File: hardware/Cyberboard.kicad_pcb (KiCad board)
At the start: 2 copper layers, 21 x 51 mm, 60 parts, among them CN1 B2B-XH-A (LF)(SN), J1 Conn_01x20, J2 Conn_01x20, SW1 SW_Push, SW2 SW_Push, U1 TPS630701RNMR, U2 NX2012SA-32.768KHZ-STD-MUB-2, U3 XL-1005UBC_C22355736, U5 BQ24074RGT, U6 STM32WB55CGUx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

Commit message: finished layout
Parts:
- removed U6: STM32WB55CGUx, Package_DFN_QFN:QFN-48-1EP_7x7mm_P0.5mm_EP5.6x5.6mm
- added U4: STM32WB55RGVx, Package_DFN_QFN:QFN-68-1EP_8x8mm_P0.4mm_EP6.4x6.4mm, F.Cu at (146.0, 90.9)
- C1, C10, C11, C12, C18, C19, C2, C20, C3, C4, C8, C9, LED1, R10, R3, R4, R5, R6, R7, R8, R9, U3, U5: moved to B.Cu
- C13, C5, C7: footprint Capacitor_SMD:C_0402_1005Metric -> Capacitor_SMD:C_0603_1608Metric; moved to B.Cu
- C21, C22, C25, C26, C27, C28: footprint Capacitor_SMD:C_0805_2012Metric -> Capacitor_SMD:C_0603_1608Metric
- C6: value 10nF -> 100nF; moved to B.Cu
- L1, L2: footprint Inductor_SMD:L_0603_1608Metric -> Inductor_SMD:L_0805_2012Metric; moved to B.Cu
- moved C20 114.5 mm to (145.5, 65.7), turned to 180 degrees
- moved R8 113.1 mm to (143.0, 66.6)
- moved R5 111.0 mm to (143.0, 67.6)
- moved R3 109.6 mm to (143.0, 68.7)
- moved U5 109.5 mm to (146.2, 68.8), turned to -90 degrees
- moved LED1 109.2 mm to (149.8, 69.0)
- moved R6 109.2 mm to (152.0, 69.0)
- moved C18 107.1 mm to (143.2, 70.8), turned to -90 degrees
- moved U3 105.7 mm to (149.8, 70.5), turned to 0 degrees
- moved R4 105.5 mm to (144.9, 72.1), turned to 90 degrees
- moved C19 104.7 mm to (147.0, 71.9), turned to 0 degrees
- moved R7 102.9 mm to (152.0, 70.5), turned to 0 degrees
- moved C16 100.1 mm to (141.9, 81.9)
- moved CN1 98.6 mm to (146.2, 64.0), turned to 180 degrees
- moved U2 98.6 mm to (142.7, 83.9), turned to 180 degrees
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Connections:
- J1 pad 1: unconnected-(J1-Pin_1-Pad1) -> /GPIO16
- J1 pad 10: unconnected-(J1-Pin_10-Pad10) -> /GPIO23
- J1 pad 11: unconnected-(J1-Pin_11-Pad11) -> /GPIO24
- J1 pad 12: unconnected-(J1-Pin_12-Pad12) -> /GPIO25
- J1 pad 13: unconnected-(J1-Pin_13-Pad13) -> GND
- J1 pad 14: unconnected-(J1-Pin_14-Pad14) -> /GPIO26
- J1 pad 15: unconnected-(J1-Pin_15-Pad15) -> /GPIO27
- J1 pad 16: unconnected-(J1-Pin_16-Pad16) -> +3.3V
- J1 pad 17: unconnected-(J1-Pin_17-Pad17) -> /GPIO28
- J1 pad 18: unconnected-(J1-Pin_18-Pad18) -> GND
- J1 pad 19: unconnected-(J1-Pin_19-Pad19) -> /GPIO29
- J1 pad 2: unconnected-(J1-Pin_2-Pad2) -> /GPIO17
- J1 pad 20: unconnected-(J1-Pin_20-Pad20) -> VBUS
- J1 pad 3: unconnected-(J1-Pin_3-Pad3) -> GND
- J1 pad 4: unconnected-(J1-Pin_4-Pad4) -> /GPIO18
- J1 pad 5: unconnected-(J1-Pin_5-Pad5) -> /GPIO19
- J1 pad 6: unconnected-(J1-Pin_6-Pad6) -> /GPIO20
- J1 pad 7: unconnected-(J1-Pin_7-Pad7) -> /GPIO21
- J1 pad 8: unconnected-(J1-Pin_8-Pad8) -> GND
- J1 pad 9: unconnected-(J1-Pin_9-Pad9) -> /GPIO22
- J2 pad 1: unconnected-(J2-Pin_1-Pad1) -> /GPIO15
- J2 pad 10: unconnected-(J2-Pin_10-Pad10) -> /GPIO8
- J2 pad 11: unconnected-(J2-Pin_11-Pad11) -> /GPIO7
- J2 pad 12: unconnected-(J2-Pin_12-Pad12) -> /GPIO6
- J2 pad 13: unconnected-(J2-Pin_13-Pad13) -> GND
- J2 pad 14: unconnected-(J2-Pin_14-Pad14) -> /GPIO5
- J2 pad 15: unconnected-(J2-Pin_15-Pad15) -> /GPIO4
- J2 pad 16: unconnected-(J2-Pin_16-Pad16) -> /GPIO3
- J2 pad 17: unconnected-(J2-Pin_17-Pad17) -> /GPIO2
- J2 pad 18: unconnected-(J2-Pin_18-Pad18) -> GND
- J2 pad 19: unconnected-(J2-Pin_19-Pad19) -> /GPIO1
- J2 pad 2: unconnected-(J2-Pin_2-Pad2) -> /GPIO14
- J2 pad 20: unconnected-(J2-Pin_20-Pad20) -> /GPIO0
- J2 pad 3: unconnected-(J2-Pin_3-Pad3) -> GND
- J2 pad 4: unconnected-(J2-Pin_4-Pad4) -> /GPIO13
- J2 pad 5: unconnected-(J2-Pin_5-Pad5) -> /GPIO12
- J2 pad 6: unconnected-(J2-Pin_6-Pad6) -> /GPIO11
- J2 pad 7: unconnected-(J2-Pin_7-Pad7) -> /GPIO10
- J2 pad 8: unconnected-(J2-Pin_8-Pad8) -> GND
- J2 pad 9: unconnected-(J2-Pin_9-Pad9) -> /GPIO9
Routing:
- net GND: vias 0 -> 4

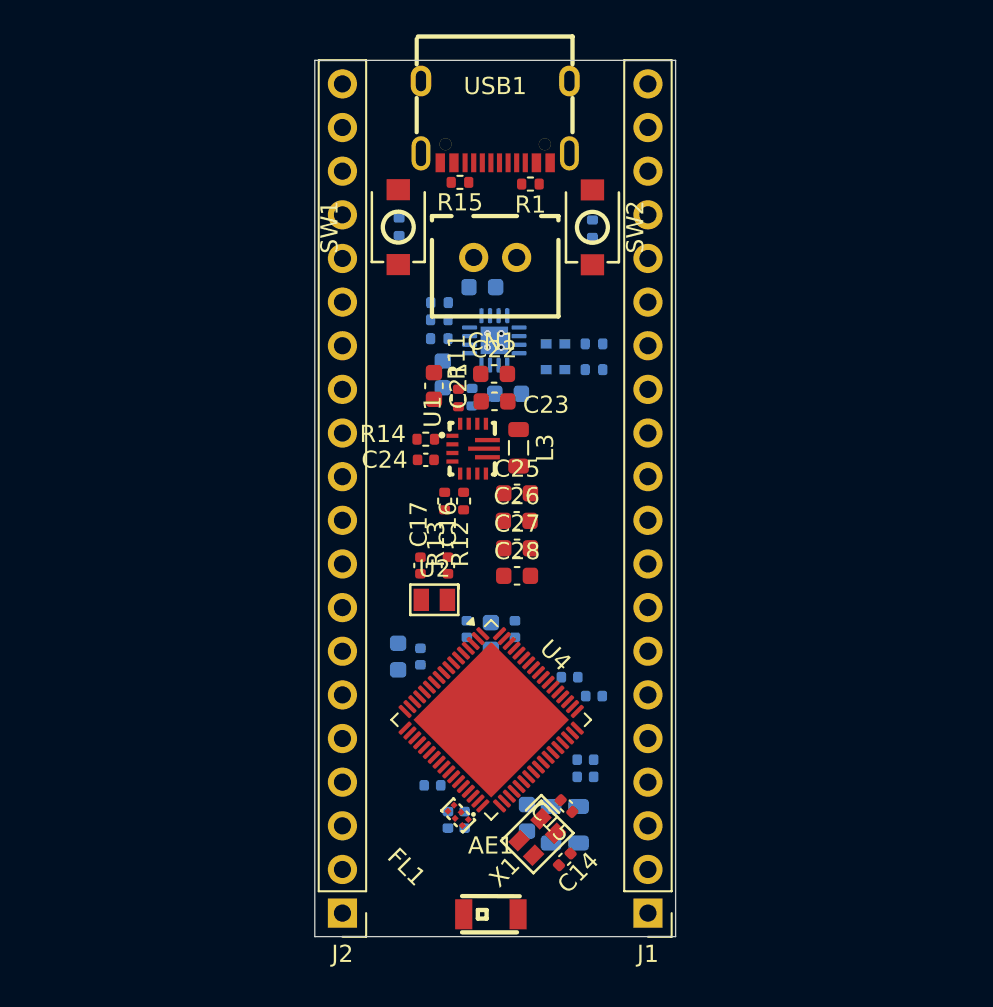
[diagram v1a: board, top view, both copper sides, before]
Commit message: add readme and also blender files
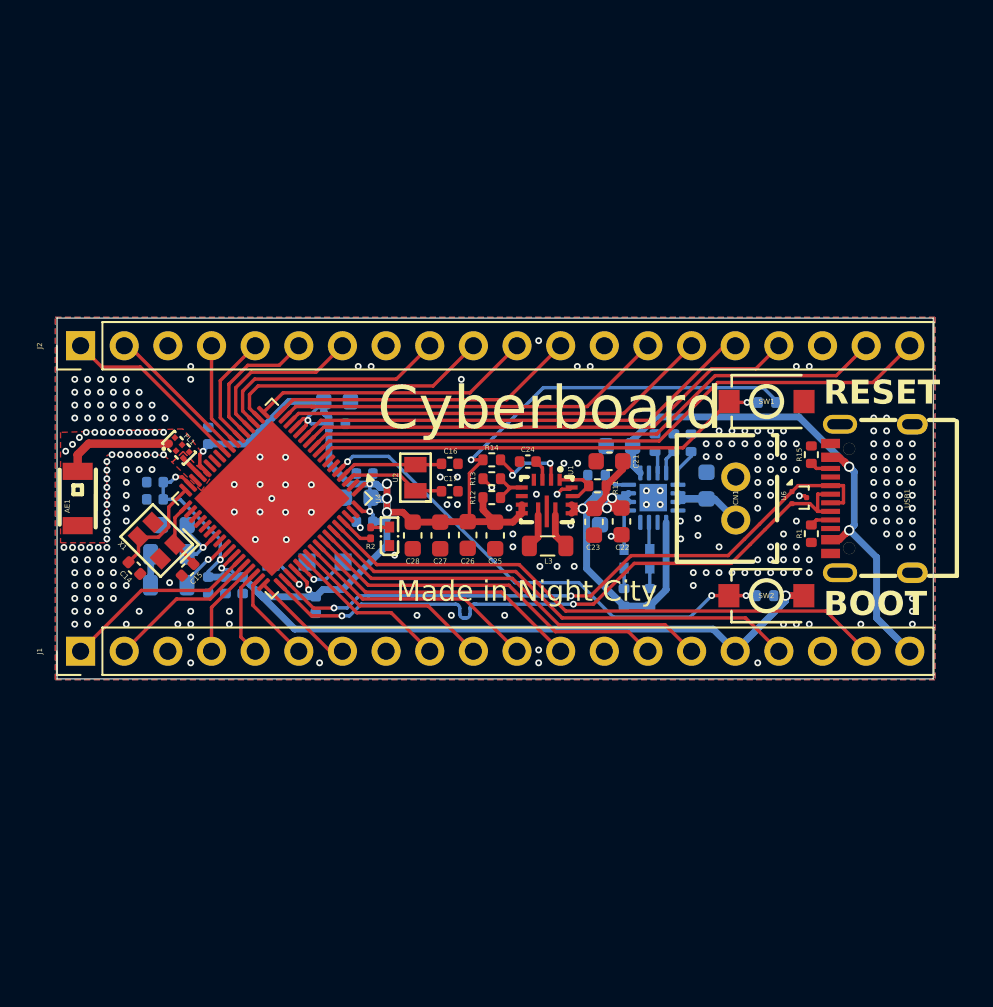
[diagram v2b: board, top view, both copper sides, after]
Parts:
- added R2: 47, Resistor_SMD:R_0201_0603Metric, F.Cu at (139.0, 80.0)
- added TP1: TestPoint, TestPoint:TestPoint_Pad_1.0x1.0mm, B.Cu at (133.2, 81.7)
- added TP2: TestPoint, TestPoint:TestPoint_Pad_1.0x1.0mm, B.Cu at (137.4, 81.7)
- added TP3: TestPoint, TestPoint:TestPoint_Pad_1.0x1.0mm, B.Cu at (135.3, 81.7)
- added U6: TPD2EUSB30, Package_TO_SOT_SMD:Texas_DRT-3, F.Cu at (163.9, 78.0)
- added U7: SZYY0402Y_C434450, lcsc:LED0402-FD_YELLOW, F.Cu at (140.1, 80.2)
- moved J2 36.4 mm to (122.1, 69.1), turned to 90 degrees
- moved J1 36.4 mm to (122.1, 86.9), turned to 90 degrees
- moved AE1 34.1 mm to (122.0, 78.0), turned to -90 degrees
- moved USB1 31.0 mm to (168.2, 78.0), turned to 90 degrees
- moved C14 30.2 mm to (125.2, 82.0), turned to -45 degrees
- moved X1 28.1 mm to (126.5, 80.5), turned to 135 degrees
- moved L1 27.6 mm to (127.2, 83.0), turned to 0 degrees
- moved L2 27.2 mm to (127.3, 81.2), turned to 180 degrees
- moved FL1 26.9 mm to (127.8, 75.0), turned to -45 degrees
- moved C13 26.7 mm to (127.5, 79.5), turned to 180 degrees
- moved R1 26.1 mm to (164.7, 80.0), turned to -90 degrees
- moved C11 26.0 mm to (126.5, 77.0), turned to 180 degrees
- moved C15 26.0 mm to (128.3, 82.2), turned to -135 degrees
- moved C10 25.9 mm to (126.5, 78.0), turned to 180 degrees
- moved R15 25.9 mm to (164.7, 75.5), turned to 90 degrees
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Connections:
- U4 pad 65: unconnected-(U4-PB5-Pad65) -> /LED
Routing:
- net +3.3V: track 0.00 -> 133.0 mm, vias 0 -> 13
- net /DN: track 0.00 -> 38.6 mm, vias 0 -> 2
- net /DP: track 0.00 -> 37.9 mm, vias 0 -> 2
- net /GPIO0: track 0.00 -> 36.9 mm
- net /GPIO1: track 0.00 -> 34.6 mm
- net /GPIO29: track 0.00 -> 33.7 mm
- net VBUS: track 0.00 -> 31.7 mm, vias 0 -> 2
- net /GPIO2: track 0.00 -> 29.6 mm
- net VCC: track 0.00 -> 29.2 mm, vias 0 -> 3
- net /BOOT: track 0.00 -> 29.1 mm, vias 0 -> 3
- net /GPIO28: track 0.00 -> 28.8 mm
- net /GPIO3: track 0.00 -> 27.3 mm
- net /RESET: track 0.00 -> 26.7 mm, vias 0 -> 1
- net /GPIO4: track 0.00 -> 25.2 mm
- net /GPIO27: track 0.00 -> 23.9 mm
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- added copper zone on B.Cu, net GND
- added copper zone on F.Cu, net GND
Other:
- board size 21 x 51 mm -> 51 x 21 mm
- board text added: "@NotARoomba"
- board text added: "BOOT"
- board text added: "CHGING"
- board text added: "Cyberboard"
- board text added: "Made in Night City"
- board text added: "READY"
- board text added: "RESET"
- board text added: "SWCLK"
- board text added: "SWD"

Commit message: add order and prod files
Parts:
- R2: value 47 -> 150
- R5: value 1.13 -> 1.13K
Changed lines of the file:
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@@
 			)
 		)
-		(property "Value" "47"
+		(property "Value" "150"
 			(at 3 0.9 90)
 			(layer "F.Fab")
@@
 			)
 		)
-		(property "Value" "1.13"
+		(property "Value" "1.13K"
 			(at 0 -1.17 90)
 			(layer "B.Fab")
@@
 				(justify mirror)
 			)
-			(render_cache "1.13" 90
+			(render_cache "1.13K" 90
 				(polygon
 					(pts
-						(xy 157.9445 74.503364) (xy 157.9445 74.458814) (xy 157.734646 74.458814) (xy 157.734646 74.408988)
-						(xy 157.692441 74.408988) (xy 157.692441 74.503364)
+						(xy 157.9445 74.39023) (xy 157.9445 74.34568) (xy 157.734646 74.34568) (xy 157.734646 74.295854)
+						(xy 157.692441 74.295854) (xy 157.692441 74.39023)
 					)
 				)
 				(polygon
 					(pts
-						(xy 157.9445 74.655478) (xy 157.9445 74.603894) (xy 157.891743 74.603894) (xy 157.891743 74.655478)
+						(xy 157.9445 74.542344) (xy 157.9445 74.49076) (xy 157.891743 74.49076) (xy 157.891743 74.542344)
 					)
 				)
 				(polygon
 					(pts
-						(xy 157.9445 74.833092) (xy 157.9445 74.788542) (xy 157.734646 74.788542) (xy 157.734646 74.738716)
-						(xy 157.692441 74.738716) (xy 157.692441 74.833092)
+						(xy 157.9445 74.719958) (xy 157.9445 74.675408) (xy 157.734646 74.675408) (xy 157.734646 74.625582)
+						(xy 157.692441 74.625582) (xy 157.692441 74.719958)
 					)
 				)
 				(polygon
 					(pts
-						(xy 157.887273 75.053203) (xy 157.853605 75.053203) (xy 157.851535 75.052782) (xy 157.842394 75.04551)
-						(xy 157.838717 75.040776) (xy 157.837814 75.037834) (xy 157.837814 75.037413) (xy 157.837814 74.98462)
-						(xy 157.795609 74.98462) (xy 157.795609 75.037725) (xy 157.795609 75.038146) (xy 157.7947 75.041106)
-						(xy 157.790993 75.045876) (xy 157.78176 75.053203) (xy 157.779654 75.053203) (xy 157.749429 75.053203)
-						(xy 157.747322 75.052782) (xy 157.737888 75.045107) (xy 157.73435 75.040379) (xy 157.733474 75.037413)
-						(xy 157.733474 74.990061) (xy 157.733895 74.988375) (xy 157.737079 74.982968) (xy 157.742505 74.976413)
-						(xy 157.748936 74.970897) (xy 157.755309 74.967822) (xy 157.743549 74.924976) (xy 157.72556 74.935051)
-						(xy 157.709092 74.950196) (xy 157.698696 74.963948) (xy 157.693046 74.976641) (xy 157.691269 74.988705)
-						(xy 157.691269 75.038201) (xy 157.692312 75.048811) (xy 157.695382 75.058528) (xy 157.700519 75.067565)
-						(xy 157.711092 75.0797) (xy 157.723618 75.090206) (xy 157.735634 75.095845) (xy 157.749264 75.097753)
-						(xy 157.780771 75.097753) (xy 157.79274 75.096009) (xy 157.804526 75.090616) (xy 157.816492 75.080937)
-						(xy 157.828451 75.090589) (xy 157.840359 75.095996) (xy 157.852579 75.097753) (xy 157.887786 75.097753)
-						(xy 157.901398 75.095845) (xy 157.913395 75.090206) (xy 157.92554 75.07949) (xy 157.936439 75.067565)
-						(xy 157.941566 75.058529) (xy 157.94463 75.048812) (xy 157.945672 75.038201) (xy 157.945672 74.988705)
-						(xy 157.94385 74.976228) (xy 157.938113 74.963384) (xy 157.927649 74.949757) (xy 157.911179 74.935051)
-						(xy 157.900508 74.928054) (xy 157.89308 74.924555) (xy 157.881851 74.967401) (xy 157.896679 74.979139)
-						(xy 157.903467 74.987972) (xy 157.903467 74.990061) (xy 157.903467 75.037725) (xy 157.90261 75.04037)
-						(xy 157.898905 75.045253) (xy 157.889343 75.053203)
+						(xy 157.887273 74.940069) (xy 157.853605 74.940069) (xy 157.851535 74.939648) (xy 157.842394 74.932376)
+						(xy 157.838717 74.927642) (xy 157.837814 74.9247) (xy 157.837814 74.924279) (xy 157.837814 74.871486)
+						(xy 157.795609 74.871486) (xy 157.795609 74.924591) (xy 157.795609 74.925012) (xy 157.7947 74.927972)
+						(xy 157.790993 74.932742) (xy 157.78176 74.940069) (xy 157.779654 74.940069) (xy 157.749429 74.940069)
+						(xy 157.747322 74.939648) (xy 157.737888 74.931973) (xy 157.73435 74.927245) (xy 157.733474 74.924279)
+						(xy 157.733474 74.876927) (xy 157.733895 74.875241) (xy 157.737079 74.869834) (xy 157.742505 74.863279)
+						(xy 157.748936 74.857763) (xy 157.755309 74.854688) (xy 157.743549 74.811842) (xy 157.72556 74.821917)
+						(xy 157.709092 74.837062) (xy 157.698696 74.850814) (xy 157.693046 74.863507) (xy 157.691269 74.875571)
+						(xy 157.691269 74.925067) (xy 157.692312 74.935677) (xy 157.695382 74.945394) (xy 157.700519 74.954431)
+						(xy 157.711092 74.966566) (xy 157.723618 74.977072) (xy 157.735634 74.982711) (xy 157.749264 74.984619)
+						(xy 157.780771 74.984619) (xy 157.79274 74.982875) (xy 157.804526 74.977482) (xy 157.816492 74.967803)
+						(xy 157.828451 74.977455) (xy 157.840359 74.982862) (xy 157.852579 74.984619) (xy 157.887786 74.984619)
+						(xy 157.901398 74.982711) (xy 157.913395 74.977072) (xy 157.92554 74.966356) (xy 157.936439 74.954431)
+						(xy 157.941566 74.945395) (xy 157.94463 74.935678) (xy 157.945672 74.925067) (xy 157.945672 74.875571)
+						(xy 157.94385 74.863094) (xy 157.938113 74.85025) (xy 157.927649 74.836623) (xy 157.911179 74.821917)
+						(xy 157.900508 74.81492) (xy 157.89308 74.811421) (xy 157.881851 74.854267) (xy 157.896679 74.866005)
+						(xy 157.903467 74.874838) (xy 157.903467 74.876927) (xy 157.903467 74.924591) (xy 157.90261 74.927236)
+						(xy 157.898905 74.932119) (xy 157.889343 74.940069)
+					)
+				)
+				(polygon
+					(pts
+						(xy 157.9445 75.228545) (xy 157.9445 75.174378) (xy 157.838987 75.087421) (xy 157.838987 75.082805)
+						(xy 157.9445 75.082805) (xy 157.9445 75.038255) (xy 157.692441 75.038255) (xy 157.692441 75.082805)
+						(xy 157.796781 75.082805) (xy 157.796781 75.087018) (xy 157.74397 75.13111) (xy 157.692441 75.173956)
+						(xy 157.692441 75.228123) (xy 157.817664 75.123545) (xy 157.874322 75.170366)
 					)
 				)

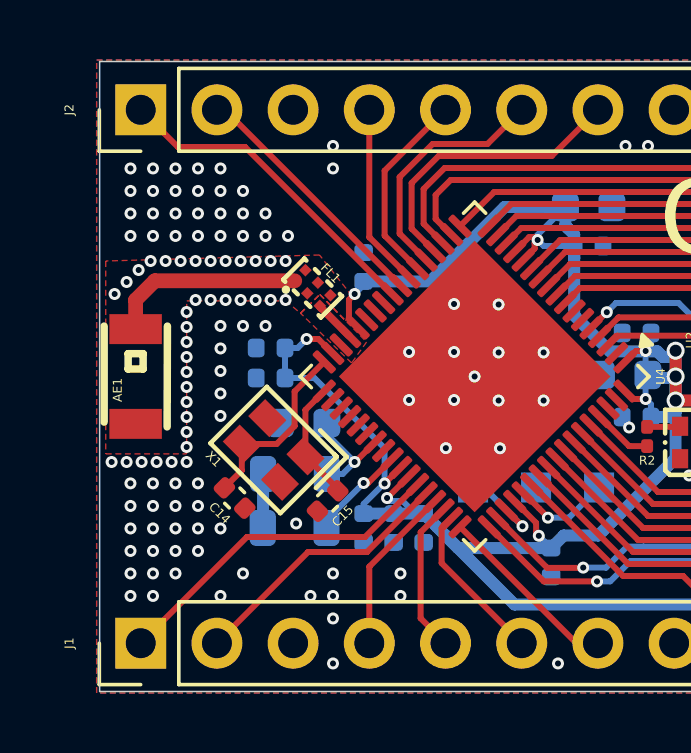
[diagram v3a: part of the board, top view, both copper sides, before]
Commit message: resized keep out
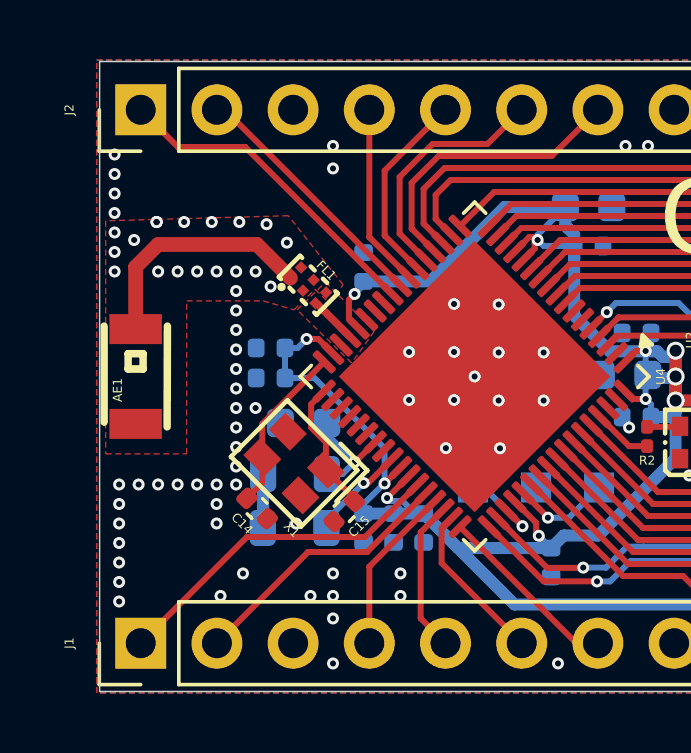
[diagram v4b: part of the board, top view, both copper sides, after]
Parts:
- moved C14 0.83 mm to (126.0, 82.4)
- moved X1 0.82 mm to (127.2, 80.9)
- moved C15 0.65 mm to (128.9, 82.5)
- moved FL1 0.17 mm to (127.7, 75.0)
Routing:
- net Net-(AE1-ANT): track 6.54 -> 8.01 mm
- net /HXOUT: track 6.27 -> 5.62 mm
- net GND: vias 253 -> 210
